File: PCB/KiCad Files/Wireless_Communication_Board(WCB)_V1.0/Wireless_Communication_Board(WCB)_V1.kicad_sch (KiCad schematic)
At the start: 7 parts, among them J1 S1, J2 S2, J3 S3, J4 S4, J5 S5, J6 Screw_Terminal_01x02, U1 LilyGo_TTGO_T7_V1.5

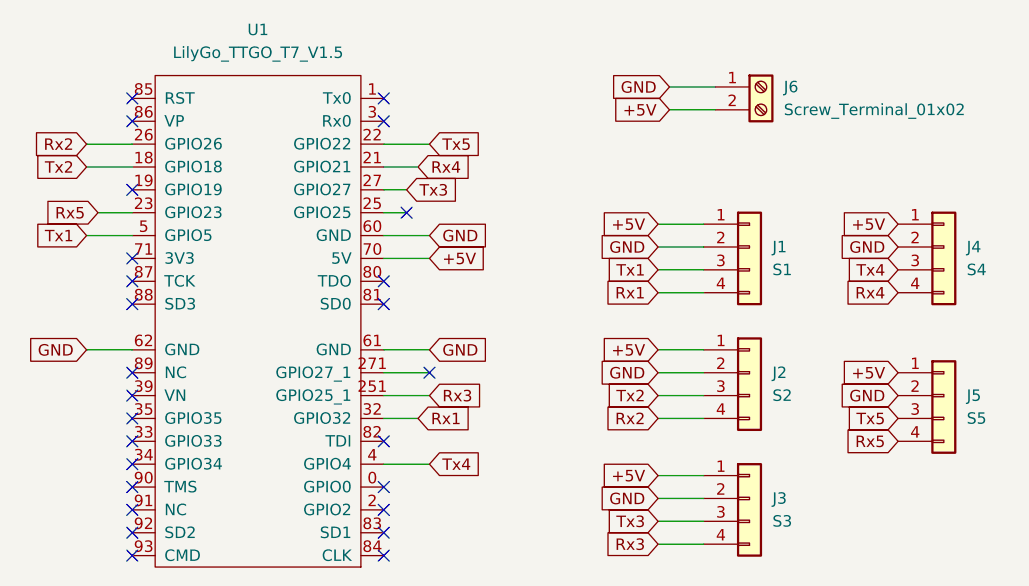
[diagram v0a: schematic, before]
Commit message: Updating the code to allow the changing of the baud rate via command line
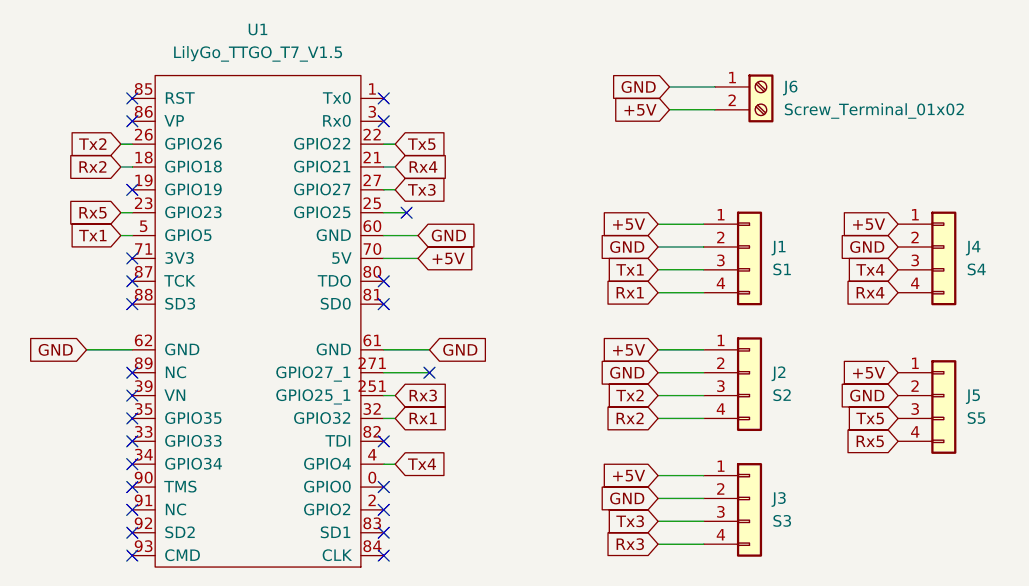
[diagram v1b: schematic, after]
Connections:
- net Rx2: now also U1.18 (GPIO18); no longer U1.26 (GPIO26)
- net Tx2: now also U1.26 (GPIO26); no longer U1.18 (GPIO18)
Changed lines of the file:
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@@
     (stroke (width 0) (type default) (color 0 0 0 0))
   )
-  (wire (pts (xy 71.12 72.39) (xy 74.93 72.39))
+  (wire (pts (xy 73.66 72.39) (xy 74.93 72.39))
     (stroke (width 0) (type default) (color 0 0 0 0))
   )
@@
     (stroke (width 0) (type default) (color 0 0 0 0))
   )
-  (wire (pts (xy 106.68 67.31) (xy 102.87 67.31))
-    (stroke (width 0) (type default) (color 0 0 0 0))
-  )
-  (wire (pts (xy 105.41 69.85) (xy 102.87 69.85))
-    (stroke (width 0) (type default) (color 0 0 0 0))
-  )
-  (wire (pts (xy 107.95 74.93) (xy 102.87 74.93))
-    (stroke (width 0) (type default) (color 0 0 0 0))
-  )
-  (wire (pts (xy 107.95 100.33) (xy 102.87 100.33))
+  (wire (pts (xy 104.14 69.85) (xy 102.87 69.85))
+    (stroke (width 0) (type default) (color 0 0 0 0))
+  )
+  (wire (pts (xy 106.68 74.93) (xy 102.87 74.93))
+    (stroke (width 0) (type default) (color 0 0 0 0))
+  )
+  (wire (pts (xy 104.14 100.33) (xy 102.87 100.33))
     (stroke (width 0) (type default) (color 0 0 0 0))
   )
@@
     (stroke (width 0) (type default) (color 0 0 0 0))
   )
-  (wire (pts (xy 107.95 77.47) (xy 102.87 77.47))
+  (wire (pts (xy 106.68 77.47) (xy 102.87 77.47))
     (stroke (width 0) (type default) (color 0 0 0 0))
   )
@@
     (stroke (width 0) (type default) (color 0 0 0 0))
   )
-  (wire (pts (xy 69.85 67.31) (xy 74.93 67.31))
+  (wire (pts (xy 73.66 67.31) (xy 74.93 67.31))
     (stroke (width 0) (type default) (color 0 0 0 0))
   )
@@
     (stroke (width 0) (type default) (color 0 0 0 0))
   )
-  (wire (pts (xy 107.95 64.77) (xy 102.87 64.77))
+  (wire (pts (xy 104.14 64.77) (xy 102.87 64.77))
     (stroke (width 0) (type default) (color 0 0 0 0))
   )
@@
     (stroke (width 0) (type default) (color 0 0 0 0))
   )
-  (wire (pts (xy 69.85 64.77) (xy 74.93 64.77))
+  (wire (pts (xy 73.66 64.77) (xy 74.93 64.77))
     (stroke (width 0) (type default) (color 0 0 0 0))
   )
@@
     (stroke (width 0) (type default) (color 0 0 0 0))
   )
-  (wire (pts (xy 106.68 95.25) (xy 102.87 95.25))
-    (stroke (width 0) (type default) (color 0 0 0 0))
-  )
-  (wire (pts (xy 107.95 92.71) (xy 102.87 92.71))
+  (wire (pts (xy 104.14 95.25) (xy 102.87 95.25))
+    (stroke (width 0) (type default) (color 0 0 0 0))
+  )
+  (wire (pts (xy 104.14 92.71) (xy 102.87 92.71))
+    (stroke (width 0) (type default) (color 0 0 0 0))
+  )
+  (wire (pts (xy 104.14 67.31) (xy 102.87 67.31))
     (stroke (width 0) (type default) (color 0 0 0 0))
   )
@@
     (stroke (width 0) (type default) (color 0 0 0 0))
   )
-  (wire (pts (xy 69.85 74.93) (xy 74.93 74.93))
+  (wire (pts (xy 73.66 74.93) (xy 74.93 74.93))
     (stroke (width 0) (type default) (color 0 0 0 0))
   )
@@
     (stroke (width 0) (type default) (color 0 0 0 0))
   )
-  (global_label "Rx1" (shape input) (at 106.68 95.25 0) (fields_autoplaced)
-    (effects (font (size 1.27 1.27)) (justify left))
-    (property "Intersheet References" "${INTERSHEET_REFS}" (id 0) (at 112.6007 95.1706 0)
+  (global_label "Rx1" (shape input) (at 104.14 95.25 0) (fields_autoplaced)
+    (effects (font (size 1.27 1.27)) (justify left))
+    (property "Intersheet References" "${INTERSHEET_REFS}" (id 0) (at 110.0607 95.1706 0)
       (effects (font (size 1.27 1.27)) (justify left) hide)
     )
@@
     )
   )
-  (global_label "Rx3" (shape input) (at 107.95 92.71 0) (fields_autoplaced)
-    (effects (font (size 1.27 1.27)) (justify left))
-    (property "Intersheet References" "${INTERSHEET_REFS}" (id 0) (at 113.8707 92.6306 0)
+  (global_label "Rx3" (shape input) (at 104.14 92.71 0) (fields_autoplaced)
+    (effects (font (size 1.27 1.27)) (justify left))
+    (property "Intersheet References" "${INTERSHEET_REFS}" (id 0) (at 110.0607 92.6306 0)
       (effects (font (size 1.27 1.27)) (justify left) hide)
     )
@@
     )
   )
-  (global_label "Tx2" (shape input) (at 69.85 67.31 180) (fields_autoplaced)
-    (effects (font (size 1.27 1.27)) (justify right))
-    (property "Intersheet References" "${INTERSHEET_REFS}" (id 0) (at 64.2317 67.2306 0)
+  (global_label "Tx2" (shape input) (at 73.66 64.77 180) (fields_autoplaced)
+    (effects (font (size 1.27 1.27)) (justify right))
+    (property "Intersheet References" "${INTERSHEET_REFS}" (id 0) (at 68.0417 64.6906 0)
       (effects (font (size 1.27 1.27)) (justify right) hide)
     )
@@
     )
   )
-  (global_label "Rx5" (shape input) (at 71.12 72.39 180) (fields_autoplaced)
-    (effects (font (size 1.27 1.27)) (justify right))
-    (property "Intersheet References" "${INTERSHEET_REFS}" (id 0) (at 65.1993 72.3106 0)
-      (effects (font (size 1.27 1.27)) (justify right) hide)
-    )
-  )
-  (global_label "+5V" (shape input) (at 107.95 77.47 0) (fields_autoplaced)
-    (effects (font (size 1.27 1.27)) (justify left))
-    (property "Intersheet References" "${INTERSHEET_REFS}" (id 0) (at 114.2336 77.5494 0)
-      (effects (font (size 1.27 1.27)) (justify left) hide)
-    )
-  )
-  (global_label "Tx5" (shape input) (at 107.95 64.77 0) (fields_autoplaced)
-    (effects (font (size 1.27 1.27)) (justify left))
-    (property "Intersheet References" "${INTERSHEET_REFS}" (id 0) (at 113.5683 64.8494 0)
-      (effects (font (size 1.27 1.27)) (justify left) hide)
-    )
-  )
-  (global_label "Rx4" (shape input) (at 106.68 67.31 0) (fields_autoplaced)
-    (effects (font (size 1.27 1.27)) (justify left))
-    (property "Intersheet References" "${INTERSHEET_REFS}" (id 0) (at 112.6007 67.3894 0)
+  (global_label "Rx5" (shape input) (at 73.66 72.39 180) (fields_autoplaced)
+    (effects (font (size 1.27 1.27)) (justify right))
+    (property "Intersheet References" "${INTERSHEET_REFS}" (id 0) (at 67.7393 72.3106 0)
+      (effects (font (size 1.27 1.27)) (justify right) hide)
+    )
+  )
+  (global_label "+5V" (shape input) (at 106.68 77.47 0) (fields_autoplaced)
+    (effects (font (size 1.27 1.27)) (justify left))
+    (property "Intersheet References" "${INTERSHEET_REFS}" (id 0) (at 112.9636 77.5494 0)
+      (effects (font (size 1.27 1.27)) (justify left) hide)
+    )
+  )
+  (global_label "Tx5" (shape input) (at 104.14 64.77 0) (fields_autoplaced)
+    (effects (font (size 1.27 1.27)) (justify left))
+    (property "Intersheet References" "${INTERSHEET_REFS}" (id 0) (at 109.7583 64.8494 0)
+      (effects (font (size 1.27 1.27)) (justify left) hide)
+    )
+  )
+  (global_label "Rx4" (shape input) (at 104.14 67.31 0) (fields_autoplaced)
+    (effects (font (size 1.27 1.27)) (justify left))
+    (property "Intersheet References" "${INTERSHEET_REFS}" (id 0) (at 110.0607 67.3894 0)
       (effects (font (size 1.27 1.27)) (justify left) hide)
     )
@@
     )
   )
-  (global_label "Tx3" (shape input) (at 105.41 69.85 0) (fields_autoplaced)
-    (effects (font (size 1.27 1.27)) (justify left))
-    (property "Intersheet References" "${INTERSHEET_REFS}" (id 0) (at 111.0283 69.7706 0)
-      (effects (font (size 1.27 1.27)) (justify left) hide)
-    )
-  )
-  (global_label "Tx1" (shape input) (at 69.85 74.93 180) (fields_autoplaced)
-    (effects (font (size 1.27 1.27)) (justify right))
-    (property "Intersheet References" "${INTERSHEET_REFS}" (id 0) (at 64.2317 75.0094 0)
+  (global_label "Tx3" (shape input) (at 104.14 69.85 0) (fields_autoplaced)
+    (effects (font (size 1.27 1.27)) (justify left))
+    (property "Intersheet References" "${INTERSHEET_REFS}" (id 0) (at 109.7583 69.7706 0)
+      (effects (font (size 1.27 1.27)) (justify left) hide)
+    )
+  )
+  (global_label "Tx1" (shape input) (at 73.66 74.93 180) (fields_autoplaced)
+    (effects (font (size 1.27 1.27)) (justify right))
+    (property "Intersheet References" "${INTERSHEET_REFS}" (id 0) (at 68.0417 75.0094 0)
       (effects (font (size 1.27 1.27)) (justify right) hide)
     )
@@
     )
   )
-  (global_label "Rx2" (shape input) (at 69.85 64.77 180) (fields_autoplaced)
-    (effects (font (size 1.27 1.27)) (justify right))
-    (property "Intersheet References" "${INTERSHEET_REFS}" (id 0) (at 63.9293 64.6906 0)
+  (global_label "Rx2" (shape input) (at 73.66 67.31 180) (fields_autoplaced)
+    (effects (font (size 1.27 1.27)) (justify right))
+    (property "Intersheet References" "${INTERSHEET_REFS}" (id 0) (at 67.7393 67.2306 0)
       (effects (font (size 1.27 1.27)) (justify right) hide)
     )
@@
     )
   )
-  (global_label "Tx4" (shape input) (at 107.95 100.33 0) (fields_autoplaced)
-    (effects (font (size 1.27 1.27)) (justify left))
-    (property "Intersheet References" "${INTERSHEET_REFS}" (id 0) (at 113.5683 100.4094 0)
+  (global_label "Tx4" (shape input) (at 104.14 100.33 0) (fields_autoplaced)
+    (effects (font (size 1.27 1.27)) (justify left))
+    (property "Intersheet References" "${INTERSHEET_REFS}" (id 0) (at 109.7583 100.4094 0)
       (effects (font (size 1.27 1.27)) (justify left) hide)
     )
@@
     )
   )
-  (global_label "GND" (shape input) (at 107.95 74.93 0) (fields_autoplaced)
-    (effects (font (size 1.27 1.27)) (justify left))
-    (property "Intersheet References" "${INTERSHEET_REFS}" (id 0) (at 114.2336 75.0094 0)
-      (effects (font (size 1.27 1.27)) (justify left) hide)
-    )
+  (global_label "GND" (shape input) (at 106.68 74.93 0) (fields_autoplaced)
+    (effects (font (size 1.27 1.27)) (justify left))
+    (property "Intersheet References" "${INTERSHEET_REFS}" (id 0) (at 112.9636 75.0094 0)
+      (effects (font (size 1.27 1.27)) (justify left) hide)
+    )
